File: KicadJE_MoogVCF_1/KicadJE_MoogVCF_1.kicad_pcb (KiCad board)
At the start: 2 copper layers, 100 x 100 mm, 213 parts, among them J201 In_Accent, J202 In Gate, J203 Out Tom, J301 Noise_In, J302 In_Accent, J303 In Gate, J304 Out Tom, P201 Doepfer_Power_10pin, P301 Doepfer_Power_10pin, Q201 MMBT2222A, Q202 MMBT2222A, Q203 MMBT2222A, Q204 MMBT2222A, Q205 MMBT2907A, Q206 MMBT2222A, Q207 MMBT2222A, Q301 MMBT2222A, Q302 MMBT2222A, Q303 MMBT2222A, Q304 MMBT2907A, Q305 MMBT2222A, Q306 MMBT2222A, SW201 Con/Tom, SW301 Con/Tom, U201 TL072, U202 TL072, U203 TL072, U301 TL072, U302 TL072

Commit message: Footprints
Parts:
- removed C201, C202, C203, C204, C302, C303, C305, C306: 100n, Capacitor_SMD:C_0805_2012Metric_Pad1.15x1.40mm_HandSolder
- removed C205, C311: 39n, Capacitor_SMD:C_0805_2012Metric_Pad1.15x1.40mm_HandSolder
- removed C206: 1u, Capacitor_SMD:C_0805_2012Metric_Pad1.15x1.40mm_HandSolder
- removed C207: 22u, Capacitor_SMD:C_0805_2012Metric_Pad1.15x1.40mm_HandSolder
- removed C208: 18n, Capacitor_SMD:C_0805_2012Metric_Pad1.15x1.40mm_HandSolder
- removed C209: C11, Capacitor_SMD:C_0805_2012Metric_Pad1.15x1.40mm_HandSolder
- removed C210: C9, Capacitor_SMD:C_0805_2012Metric_Pad1.15x1.40mm_HandSolder
- removed C211: C10, Capacitor_SMD:C_0805_2012Metric_Pad1.15x1.40mm_HandSolder
- removed C212, C310: 1n, Capacitor_SMD:C_0805_2012Metric_Pad1.15x1.40mm_HandSolder
- removed C213: C12, Capacitor_SMD:C_0805_2012Metric_Pad1.15x1.40mm_HandSolder
- removed C214: C8, Capacitor_SMD:C_0805_2012Metric_Pad1.15x1.40mm_HandSolder
- removed C215: C6, Capacitor_SMD:C_0805_2012Metric_Pad1.15x1.40mm_HandSolder
- removed C216, C314: 47n, Capacitor_SMD:C_0805_2012Metric_Pad1.15x1.40mm_HandSolder
- removed C217, C315: 10n, Capacitor_SMD:C_0805_2012Metric_Pad1.15x1.40mm_HandSolder
- removed C218: C7, Capacitor_SMD:C_0805_2012Metric_Pad1.15x1.40mm_HandSolder
- removed C219: C4, Capacitor_SMD:C_0805_2012Metric_Pad1.15x1.40mm_HandSolder
- removed C220, C221, C301, C304: 10u, Capacitor_SMD:C_1206_3216Metric_Pad1.42x1.75mm_HandSolder
- removed C307, C308: 27n, Capacitor_SMD:C_0805_2012Metric_Pad1.15x1.40mm_HandSolder
- removed C309: 12n, Capacitor_SMD:C_0805_2012Metric_Pad1.15x1.40mm_HandSolder
- removed C312: 2n7, Capacitor_SMD:C_0805_2012Metric_Pad1.15x1.40mm_HandSolder
- removed C313, C317: 33n, Capacitor_SMD:C_0805_2012Metric_Pad1.15x1.40mm_HandSolder
- removed C316: 15n, Capacitor_SMD:C_0805_2012Metric_Pad1.15x1.40mm_HandSolder
- removed D201, D202, D301, D302: 1N1007, Diode_SMD:D_SOD-123
- removed D203, D204: D_Zener, Diode_SMD:D_MiniMELF
- removed D205, D206, D207, D208, D209, D312: 1N4148, Diode_SMD:D_SOD-123
- removed D303, D304, D305, D306, D307, D308: Zener, Diode_SMD:D_MiniMELF
- removed D309, D310, D311, D313: 1N4148, Diode_SMD:D_MiniMELF
- removed H204, H303, H304: 2,2mm, MountingHole:MountingHole_2.2mm_M2_Pad_Via
- removed H301, H302: 2,5mm, MountingHole:MountingHole_2.5mm_Pad_Via
- removed J201, J302: In_Accent, Connector_Audio:Jack_3.5mm_Ledino_KB3SPRS_Horizontal
- removed J202, J303: In Gate, AJ-Dropbox-Kicad:PJ301SM
- removed J203, J304: Out Tom, AJ-Dropbox-Kicad:PJ301SM
- removed J301: Noise_In, AJ-Dropbox-Kicad:PJ301SM
- removed JP201: Jumper, Connector_PinHeader_2.54mm:PinHeader_1x02_P2.54mm_Vertical
- removed P201, P301: Doepfer_Power_10pin, Connectors_IDC:IDC-Header_2x05_Pitch2.54mm_Straight
- removed Q201, Q202, Q203, Q204, Q206, Q207, Q301, Q302, Q303, Q305, Q306: MMBT2222A, Package_TO_SOT_SMD:SOT-23_Handsoldering
- removed Q205, Q304: MMBT2907A, Package_TO_SOT_SMD:SOT-23_Handsoldering
- removed R201, R206: 1M, Resistor_SMD:R_0805_2012Metric_Pad1.15x1.40mm_HandSolder
- removed R202, R220, R221, R228, R229, R233, R235, R238, R239, R242, R314, R315, R322, R323, R327, R329, R332, R333, R336: 4k7, Resistor_SMD:R_0805_2012Metric_Pad1.15x1.40mm_HandSolder
- removed R203: 330K, Resistor_SMD:R_0805_2012Metric_Pad1.15x1.40mm_HandSolder
- removed R204: 100R, Resistor_SMD:R_0805_2012Metric_Pad1.15x1.40mm_HandSolder
- removed R205, R207, R232, R240, R241, R245, R250, R326, R334, R335, R339, R344: 22k, Resistor_SMD:R_0805_2012Metric_Pad1.15x1.40mm_HandSolder
- removed R208: 300R, Resistor_SMD:R_0805_2012Metric_Pad1.15x1.40mm_HandSolder
- removed R209, R211, R301, R302, R305: 1K, Resistor_SMD:R_0805_2012Metric_Pad1.15x1.40mm_HandSolder
- removed R210, R213, R303, R304, R306: OPEN, Resistor_SMD:R_0805_2012Metric_Pad1.15x1.40mm_HandSolder
- removed R212, R307: 0R, Resistor_SMD:R_0805_2012Metric_Pad1.15x1.40mm_HandSolder
- removed R214, R225, R308, R319: 1k, Resistor_SMD:R_0805_2012Metric_Pad1.15x1.40mm_HandSolder
- removed R215, R222, R309, R316: 470k, Resistor_SMD:R_0805_2012Metric_Pad1.15x1.40mm_HandSolder
- removed R216, R310: 820k, Resistor_SMD:R_0805_2012Metric_Pad1.15x1.40mm_HandSolder
- removed R217, R223, R244, R249, R311, R317, R338, R343: 33k, Resistor_SMD:R_0805_2012Metric_Pad1.15x1.40mm_HandSolder
- removed R218, R219, R224, R234, R251, R252, R253, R254, R312, R313, R318, R328, R345, R346, R347, R348: 100k, Resistor_SMD:R_0805_2012Metric_Pad1.15x1.40mm_HandSolder
- removed R226, R320: 15k, Resistor_SMD:R_0805_2012Metric_Pad1.15x1.40mm_HandSolder
- removed R227, R236, R237, R246, R321, R330, R331, R340: 10k, Resistor_SMD:R_0805_2012Metric_Pad1.15x1.40mm_HandSolder
- removed R230: R17, Resistor_SMD:R_0805_2012Metric_Pad1.15x1.40mm_HandSolder
- removed R231: R18, Resistor_SMD:R_0805_2012Metric_Pad1.15x1.40mm_HandSolder
- removed R243, R337: 3k3, Resistor_SMD:R_0805_2012Metric_Pad1.15x1.40mm_HandSolder
- removed R247, R341: 47k, Resistor_SMD:R_0805_2012Metric_Pad1.15x1.40mm_HandSolder
- removed R248, R342: 2M2, Resistor_SMD:R_0805_2012Metric_Pad1.15x1.40mm_HandSolder
- removed R324: 2k5, Resistor_SMD:R_0805_2012Metric_Pad1.15x1.40mm_HandSolder
- removed R325: 6k8, Resistor_SMD:R_0805_2012Metric_Pad1.15x1.40mm_HandSolder
- removed RV201: 100K, Potentiometer_THT:Potentiometer_Bourns_3296W_Vertical
- removed RV202: 50K, Potentiometer_THT:Potentiometer_Bourns_3296W_Vertical
- removed RV203, RV301: 500R Tune, Potentiometer_THT:Potentiometer_Piher_T-16H_Single_Horizontal
- removed RV204, RV302: 1M Decay, Potentiometer_THT:Potentiometer_Piher_T-16H_Single_Horizontal
- removed RV205, RV303: 100k A Level, Potentiometer_THT:Potentiometer_Piher_T-16H_Single_Horizontal
- removed RV206, RV304: 100k A Reverb, Potentiometer_THT:Potentiometer_Piher_T-16H_Single_Horizontal
- removed SW201, SW301: Con/Tom, AJ-Dropbox-Kicad:SPDTx2
- removed TP201: WhiteNoise, TestPoint:TestPoint_Pad_1.5x1.5mm
- removed TP202: GND, TestPoint:TestPoint_THTPad_2.0x2.0mm_Drill1.0mm
- removed TP203, TP301: Coupling, TestPoint:TestPoint_Pad_1.5x1.5mm
- removed U201, U202, U203, U301, U302: TL072, AJ-Dropbox-Kicad:AJ_SO-8_5.3x6.2mm_P1.27mm
- moved G*** 31.5 mm to (103.8, 168.5)
- moved G*** 31.4 mm to (97.5, 169.2)
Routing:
- net +12V: track 356.1 -> 0.00 mm, vias 2 -> 0
- net GND: track 332.3 -> 0.00 mm, vias 118 -> 0
- net -12V: track 239.6 -> 0.00 mm, vias 2 -> 0
- net Net-(C210-Pad2): track 99.5 -> 0.00 mm, vias 2 -> 0
- net Net-(C308-Pad2): track 90.0 -> 0.00 mm, vias 2 -> 0
- net Net-(C317-Pad1): track 81.0 -> 0.00 mm, vias 2 -> 0
- net Net-(C313-Pad1): track 74.3 -> 0.00 mm
- net InAccent2: track 67.9 -> 0.00 mm, vias 2 -> 0
- net Net-(R311-Pad2): track 65.0 -> 0.00 mm, vias 2 -> 0
- net /KicadJE_AteOhAte3/Coupling: track 60.1 -> 0.00 mm, vias 2 -> 0
- net Net-(C209-Pad2): track 56.0 -> 0.00 mm, vias 2 -> 0
- net Net-(C218-Pad1): track 54.1 -> 0.00 mm, vias 4 -> 0
- net Net-(C212-Pad2): track 52.9 -> 0.00 mm, vias 4 -> 0
- net Net-(C310-Pad1): track 50.2 -> 0.00 mm, vias 2 -> 0
- net Net-(C212-Pad1): track 48.4 -> 0.00 mm, vias 5 -> 0
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- removed copper zone on B.Cu, net GND
- removed copper zone on F.Cu, net GND
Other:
- outline, holes or cut-outs redrawn
- board text removed: "Reg noise to 130mV"

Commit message: Placing components
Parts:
- removed G*** (x2): LOGO, AJ:Johansen_engineering_logo_25mm_front_neg5
- added C201: 10u, Capacitor_SMD:C_1206_3216Metric_Pad1.42x1.75mm_HandSolder, B.Cu at (1.15, 103.7)
- added C202: 100n, Capacitor_SMD:C_0805_2012Metric_Pad1.15x1.40mm_HandSolder, B.Cu at (44.3, 58.0)
- added C203: 100n, Capacitor_SMD:C_0805_2012Metric_Pad1.15x1.40mm_HandSolder, B.Cu at (36.4, 64.4)
- added C204: 10u, Capacitor_SMD:C_1206_3216Metric_Pad1.42x1.75mm_HandSolder, B.Cu at (14.2, 93.5)
- added C205: 100n, Capacitor_SMD:C_0805_2012Metric_Pad1.15x1.40mm_HandSolder, B.Cu at (16.9, 82.9)
- added C206: 100n, Capacitor_SMD:C_0805_2012Metric_Pad1.15x1.40mm_HandSolder, B.Cu at (1.87, 98.3)
- added C207: 47n, Capacitor_SMD:C_0805_2012Metric_Pad1.15x1.40mm_HandSolder, B.Cu at (33.4, 65.8)
- added C208: 47n, Capacitor_SMD:C_0805_2012Metric_Pad1.15x1.40mm_HandSolder, B.Cu at (11.1, 89.3)
- added C209: 47n, Capacitor_SMD:C_0805_2012Metric_Pad1.15x1.40mm_HandSolder, B.Cu at (41.3, 58.0)
- added C210: 47n, Capacitor_SMD:C_0805_2012Metric_Pad1.15x1.40mm_HandSolder, B.Cu at (26.8, 71.8)
- added C211: 10u, Capacitor_SMD:C_0805_2012Metric_Pad1.15x1.40mm_HandSolder, B.Cu at (8.13, 92.5)
- added C212: 10u, Capacitor_SMD:C_0805_2012Metric_Pad1.15x1.40mm_HandSolder, B.Cu at (13.9, 83.4)
- added C213: Opt_220u, Capacitor_THT:CP_Radial_D10.0mm_P5.00mm, B.Cu at (40.0, 81.5)
- added C214: 22u, Capacitor_SMD:C_0805_2012Metric_Pad1.15x1.40mm_HandSolder, B.Cu at (0.53, 122.2)
- added C215: 100p, Capacitor_SMD:C_0805_2012Metric_Pad1.15x1.40mm_HandSolder, B.Cu at (24.9, 76.5)
- added D201: 1N1007, Diode_SMD:D_SOD-123, B.Cu at (20.0, 82.4)
- added D202: 1N1007, Diode_SMD:D_SOD-123, B.Cu at (30.5, 49.2)
- added D203: Zener, Diode_SMD:D_MiniMELF, B.Cu at (0.38, 127.7)
- added D204: Zener, Diode_SMD:D_MiniMELF, B.Cu at (0.38, 134.1)
- added D205: Zener, Diode_SMD:D_MiniMELF, B.Cu at (7.67, 104.0)
- added D206: Zener, Diode_SMD:D_MiniMELF, B.Cu at (23.3, 82.1)
- added D207: Zener, Diode_SMD:D_MiniMELF, B.Cu at (4.42, 104.0)
- added D208: Zener, Diode_SMD:D_MiniMELF, B.Cu at (-24.0, 103.6)
- added D209: Zener, Diode_SMD:D_MiniMELF, B.Cu at (22.7, 101.5)
- added D210: Zener, Diode_SMD:D_MiniMELF, B.Cu at (29.0, 101.5)
- added H201: 2,5mm, MountingHole:MountingHole_2.5mm_Pad_Via, B.Cu at (5.28, 122.8)
- added H202: 2,5mm, MountingHole:MountingHole_2.5mm_Pad_Via, B.Cu at (28.1, 122.8)
- added H203: 2,2mm, MountingHole:MountingHole_2.2mm_M2_Pad_Via, B.Cu at (-20.8, 97.4)
- added H204: 2,2mm, MountingHole:MountingHole_2.2mm_M2_Pad_Via, B.Cu at (-20.2, 91.0)
- added J201: CV2, AJ-Dropbox-Kicad:PJ301SM, F.Cu at (79.8, 120.0)
- added J202: Input, AJ-Dropbox-Kicad:PJ301SM, F.Cu at (59.8, 145.0)
- added J203: CV1, AJ-Dropbox-Kicad:PJ301SM, F.Cu at (79.8, 105.0)
- added J204: Out VCF, AJ-Dropbox-Kicad:PJ301SM, F.Cu at (79.8, 145.0)
- added J205: Input, AJ-Dropbox-Kicad:PJ301SM, F.Cu at (59.8, 135.0)
- added P201: Doepfer_Power_10pin, Connectors_IDC:IDC-Header_2x05_Pitch2.54mm_Straight, B.Cu at (74.8, 56.8)
- added Q201: UMX1N, AJ:UMX1N_UMT6_DualNPN, B.Cu at (31.3, 17.5)
- added Q202: SS9014, Package_TO_SOT_SMD:SOT-23_Handsoldering, B.Cu at (27.9, 19.2)
- added Q203: SS9014, Package_TO_SOT_SMD:SOT-23_Handsoldering, B.Cu at (34.8, 19.2)
- added Q204: SS9014, Package_TO_SOT_SMD:SOT-23_Handsoldering, B.Cu at (27.9, 27.5)
- added Q205: SS9014, Package_TO_SOT_SMD:SOT-23_Handsoldering, B.Cu at (34.8, 27.5)
- added Q206: SS9014, Package_TO_SOT_SMD:SOT-23_Handsoldering, B.Cu at (27.9, 34.7)
- added Q207: SS9014, Package_TO_SOT_SMD:SOT-23_Handsoldering, B.Cu at (34.8, 34.8)
- added Q208: UMX1N, AJ:UMX1N_UMT6_DualNPN, B.Cu at (31.5, 36.2)
- added Q209: UMX1N, AJ:UMX1N_UMT6_DualNPN, B.Cu at (5.50, 62.8)
- added Q210: UMX1N, AJ:UMX1N_UMT6_DualNPN, B.Cu at (0.00, 62.5)
- added Q211: SS9014, Package_TO_SOT_SMD:SOT-23_Handsoldering, B.Cu at (0.75, 33.8)
- added Q212: SS9015, Package_TO_SOT_SMD:SOT-23_Handsoldering, B.Cu at (0.75, 39.5)
- added R201: 330R, Resistor_SMD:R_0805_2012Metric_Pad1.15x1.40mm_HandSolder, B.Cu at (14.4, 88.1)
- added R202: 1K, Resistor_SMD:R_0805_2012Metric_Pad1.15x1.40mm_HandSolder, B.Cu at (27.5, 62.3)
- added R203: 1K, Resistor_SMD:R_0805_2012Metric_Pad1.15x1.40mm_HandSolder, B.Cu at (26.6, 57.5)
- added R204: OPEN, Resistor_SMD:R_0805_2012Metric_Pad1.15x1.40mm_HandSolder, B.Cu at (21.6, 62.3)
- added R205: OPEN, Resistor_SMD:R_0805_2012Metric_Pad1.15x1.40mm_HandSolder, B.Cu at (29.5, 57.5)
- added R206: 150R, Resistor_SMD:R_0805_2012Metric_Pad1.15x1.40mm_HandSolder, B.Cu at (5.18, 92.5)
- added R207: 1K, Resistor_SMD:R_0805_2012Metric_Pad1.15x1.40mm_HandSolder, B.Cu at (19.0, 77.1)
- added R208: 0R, Resistor_SMD:R_0805_2012Metric_Pad1.15x1.40mm_HandSolder, B.Cu at (30.5, 65.8)
- added R209: OPEN, Resistor_SMD:R_0805_2012Metric_Pad1.15x1.40mm_HandSolder, B.Cu at (38.4, 58.7)
- added R210: 150R, Resistor_SMD:R_0805_2012Metric_Pad1.15x1.40mm_HandSolder, B.Cu at (8.13, 87.7)
- added R211: 0R, Resistor_SMD:R_0805_2012Metric_Pad1.15x1.40mm_HandSolder, B.Cu at (23.8, 71.8)
- added R212: Open, Resistor_SMD:R_0805_2012Metric_Pad1.15x1.40mm_HandSolder, B.Cu at (26.8, 67.0)
- added R213: 150R, Resistor_SMD:R_0805_2012Metric_Pad1.15x1.40mm_HandSolder, B.Cu at (17.9, 72.4)
- added R214: 180R, Resistor_SMD:R_0805_2012Metric_Pad1.15x1.40mm_HandSolder, B.Cu at (2.23, 92.5)
- added R215: 22R, Resistor_SMD:R_0805_2012Metric_Pad1.15x1.40mm_HandSolder, B.Cu at (22.0, 76.5)
- added R216: 1k, Resistor_SMD:R_0805_2012Metric_Pad1.15x1.40mm_HandSolder, B.Cu at (5.18, 87.7)
- added R217: 120k, Resistor_SMD:R_0805_2012Metric_Pad1.15x1.40mm_HandSolder, B.Cu at (16.1, 78.1)
- added R218: 120k, Resistor_SMD:R_0805_2012Metric_Pad1.15x1.40mm_HandSolder, B.Cu at (20.9, 71.8)
- added R219: 56k, Resistor_SMD:R_0805_2012Metric_Pad1.15x1.40mm_HandSolder, B.Cu at (32.5, 61.0)
- added R220: 56k, Resistor_SMD:R_0805_2012Metric_Pad1.15x1.40mm_HandSolder, B.Cu at (-0.72, 93.6)
- added R221: 120k, Resistor_SMD:R_0805_2012Metric_Pad1.15x1.40mm_HandSolder, B.Cu at (11.0, 83.0)
- added R222: 1k, Resistor_SMD:R_0805_2012Metric_Pad1.15x1.40mm_HandSolder, B.Cu at (13.1, 78.2)
- added R223: 10k, Resistor_SMD:R_0805_2012Metric_Pad1.15x1.40mm_HandSolder, B.Cu at (23.8, 67.0)
- added R224: 150R, Resistor_SMD:R_0805_2012Metric_Pad1.15x1.40mm_HandSolder, B.Cu at (8.02, 83.0)
- added R225: 470R, Resistor_SMD:R_0805_2012Metric_Pad1.15x1.40mm_HandSolder, B.Cu at (35.4, 59.7)
- added R226: 47k, Resistor_SMD:R_0805_2012Metric_Pad1.15x1.40mm_HandSolder, B.Cu at (11.1, 94.1)
- added R227: 47k, Resistor_SMD:R_0805_2012Metric_Pad1.15x1.40mm_HandSolder, B.Cu at (2.23, 87.7)
- added R228: 1k, Resistor_SMD:R_0805_2012Metric_Pad1.15x1.40mm_HandSolder, B.Cu at (35.4, 54.9)
- added R229: 330R, Resistor_SMD:R_0805_2012Metric_Pad1.15x1.40mm_HandSolder, B.Cu at (10.2, 78.2)
- added R230: 270k, Resistor_SMD:R_0805_2012Metric_Pad1.15x1.40mm_HandSolder, B.Cu at (32.5, 56.3)
- added R231: 1k2, Resistor_SMD:R_0805_2012Metric_Pad1.15x1.40mm_HandSolder, B.Cu at (20.9, 67.0)
- added R232: 270k, Resistor_SMD:R_0805_2012Metric_Pad1.15x1.40mm_HandSolder, B.Cu at (5.07, 83.0)
- added R233: 220R, Resistor_SMD:R_0805_2012Metric_Pad1.15x1.40mm_HandSolder, B.Cu at (-0.72, 88.8)
- added R234: 100k, Resistor_SMD:R_0805_2012Metric_Pad1.15x1.40mm_HandSolder, B.Cu at (13.1, 73.5)
- added R235: 680R, Resistor_SMD:R_0805_2012Metric_Pad1.15x1.40mm_HandSolder, B.Cu at (24.6, 62.3)
- added R236: 150k, Resistor_SMD:R_0805_2012Metric_Pad1.15x1.40mm_HandSolder, B.Cu at (10.2, 73.5)
- added R237: 1k8, Resistor_SMD:R_0805_2012Metric_Pad1.15x1.40mm_HandSolder, B.Cu at (2.12, 83.0)
- added R238: 100k, Resistor_SMD:R_0805_2012Metric_Pad1.15x1.40mm_HandSolder, B.Cu at (7.22, 78.2)
- added R239: 470R, Resistor_SMD:R_0805_2012Metric_Pad1.15x1.40mm_HandSolder, B.Cu at (17.9, 67.6)
- added R240: 1K, Resistor_SMD:R_0805_2012Metric_Pad1.15x1.40mm_HandSolder, B.Cu at (21.9, 98.4)
- added R241: OPEN, Resistor_SMD:R_0805_2012Metric_Pad1.15x1.40mm_HandSolder, B.Cu at (22.5, 105.3)
- added RV201: 50k_emphasis, AJ-Dropbox-Kicad:Potentiometer_China_RK09_Single_Vertical_AJ, F.Cu at (87.0, 67.5)
- added RV202: 1k, AJ-Dropbox-Kicad:Bourns3296WV, B.Cu at (28.2, 83.6)
- added RV203: 50k_CV1, AJ-Dropbox-Kicad:Potentiometer_China_RK09_Single_Vertical_AJ, F.Cu at (52.2, 107.5)
- added RV204: 10k_Freq, AJ-Dropbox-Kicad:Potentiometer_China_RK09_Single_Vertical_AJ, F.Cu at (52.2, 72.5)
- added RV205: 500R, AJ-Dropbox-Kicad:Bourns3296WV, B.Cu at (5.33, 129.1)
- added RV206: 50k_CV2, AJ-Dropbox-Kicad:Potentiometer_China_RK09_Single_Vertical_AJ, F.Cu at (52.2, 122.5)
- added TP201: PreOut, TestPoint:TestPoint_Pad_1.5x1.5mm, B.Cu at (44.0, 53.8)
- added TP202: Input, TestPoint:TestPoint_Pad_1.5x1.5mm, B.Cu at (40.4, 53.8)
- added U201: TL072, AJ-Dropbox-Kicad:AJ_SO-8_5.3x6.2mm_P1.27mm, B.Cu at (25.5, 110.6)

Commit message: fixing links
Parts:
- added D211: LED, LED_SMD:LED_0805_2012Metric, F.Cu at (79.8, 58.3)
- added R242: 12K, Resistor_SMD:R_0805_2012Metric_Pad1.15x1.40mm_HandSolder, F.Cu at (79.8, 53.8)
- C201, C204, D201, D202: moved to F.Cu
- moved R204 80.8 mm to (79.4, 118.8)
- moved R202 79.6 mm to (79.2, 122.8)
- moved C201 78.3 mm to (65.8, 59.5), turned to 180 degrees
- moved R206 77.1 mm to (22.0, 17.2)
- moved C204 68.1 mm to (73.3, 59.5), turned to 180 degrees
- moved R210 67.4 mm to (22.0, 21.7)
- moved C208 66.8 mm to (31.5, 25.8), turned to 180 degrees
- moved R211 61.1 mm to (84.8, 67.5), turned to 270 degrees
- moved R212 58.1 mm to (84.8, 71.2)
- moved D201 55.7 mm to (66.2, 51.2), turned to 0 degrees
- moved C206 55.3 mm to (44.2, 62.7)
- moved R224 50.2 mm to (22.0, 34.7)
- moved C215 46.8 mm to (-5.75, 41.2)
- moved C207 45.8 mm to (31.2, 20.0), turned to 180 degrees
- moved R213 44.3 mm to (22.0, 28.2)
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
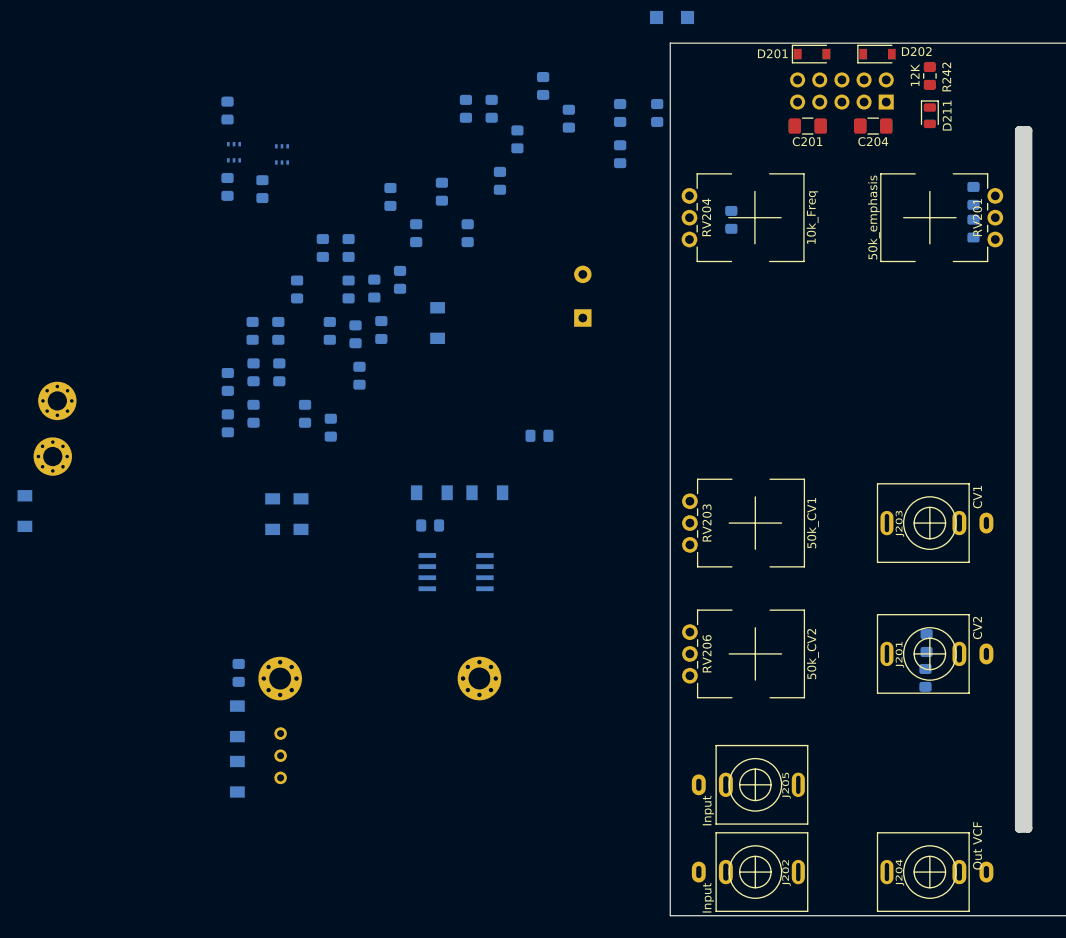
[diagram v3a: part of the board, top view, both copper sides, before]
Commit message: placing input prot
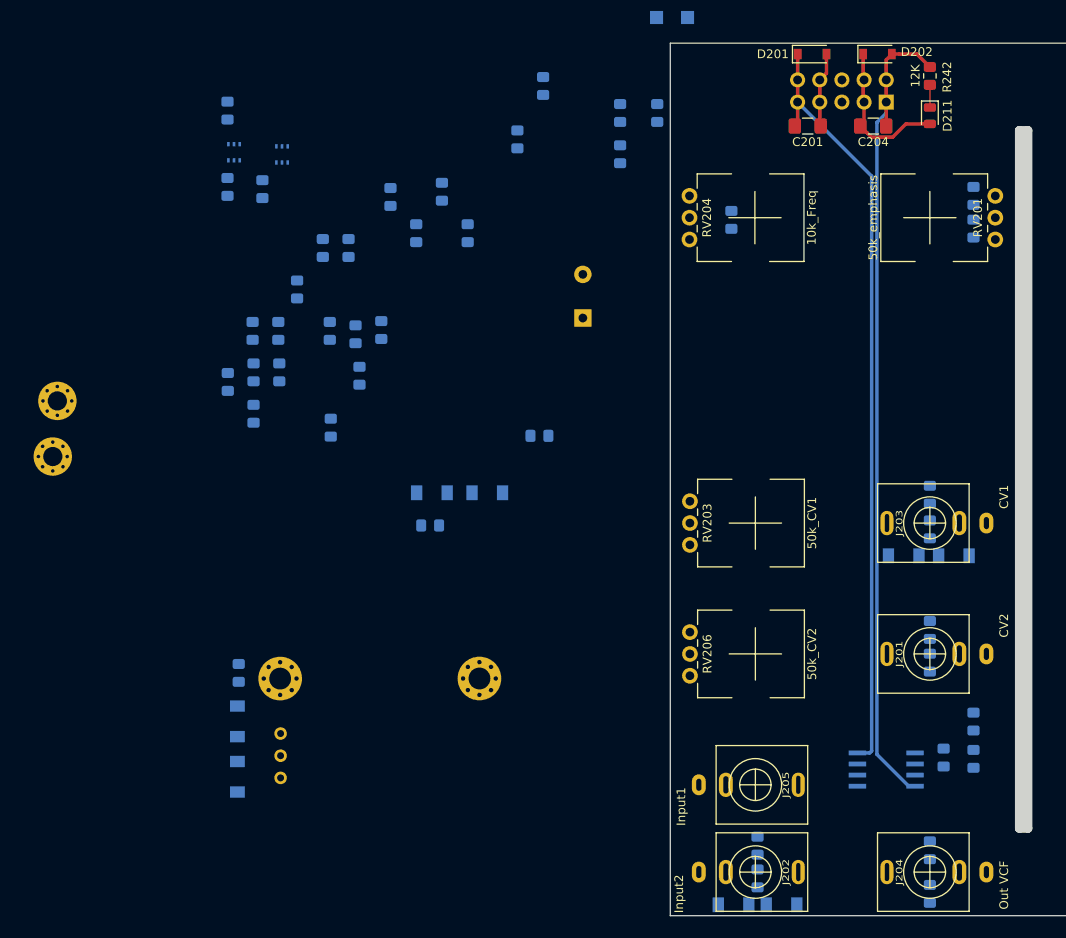
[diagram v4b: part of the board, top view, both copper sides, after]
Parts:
- J202: value Input -> Input2
- J205: value Input -> Input1
- moved D208 106.6 mm to (82.5, 108.8), turned to 180 degrees
- moved R208 95.4 mm to (79.8, 147.5)
- moved R203 94.3 mm to (60.0, 145.7)
- moved R220 93.7 mm to (84.8, 132.0), turned to 270 degrees
- moved R222 92.6 mm to (79.8, 142.5), turned to 270 degrees
- moved R205 89.8 mm to (60.0, 142.0)
- moved R217 84.5 mm to (81.3, 131.9)
- moved C211 84.3 mm to (84.8, 127.8)
- moved D206 77.5 mm to (62.8, 148.8), turned to 180 degrees
- moved D207 72.5 mm to (76.8, 108.8), turned to 0 degrees
- moved R207 67.1 mm to (79.8, 105.7)
- moved D205 66.8 mm to (57.2, 148.8), turned to 0 degrees
- moved R209 59.7 mm to (79.8, 101.8)
- moved U201 54.2 mm to (74.8, 133.2), turned to 180 degrees
- moved R202 1.82 mm to (79.8, 121.0)
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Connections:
- D205 pad 1: InAudio -> InAudio2
- D209 pad 1: InAudio -> InAudio1
- J205 pad S: (no net) -> GND
- R203 pad 2: InAudio -> InAudio2
- R205 pad 1: InAudio -> InAudio2
- R218 pad 1: (no net) -> InAudio1
- R221 pad 1: (no net) -> InAudio2
- R240 pad 2: InAudio -> InAudio1
- R241 pad 1: InAudio -> InAudio1
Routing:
- net -12V: track 0.00 -> 94.6 mm
- net +12V: track 0.00 -> 88.0 mm
- net GND: track 0.00 -> 26.2 mm
- net Net-(D211-Pad1): track 0.00 -> 2.60 mm
